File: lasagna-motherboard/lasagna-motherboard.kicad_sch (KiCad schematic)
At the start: 0 parts

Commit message: created IMU Schematic symbol
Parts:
- added U?: Adafruit_BNO055_IMU, symbol lasagna-motherboard:Adafruit_BNO055_IMU
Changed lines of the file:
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@@
 (kicad_sch (version 20211123) (generator eeschema)
   (paper "A4")
+  (symbol (lib_id "lasagna-motherboard:Adafruit_BNO055_IMU") (at 34.29 34.29 0) (unit 1)
+    (in_bom yes) (on_board yes) (fields_autoplaced)
+    (property "Reference" "U?" (id 0) (at 33.655 20.32 0))
+    (property "Value" "Adafruit_BNO055_IMU" (id 1) (at 33.655 22.86 0))
+    (property "Footprint" "" (id 2) (at 30.48 33.02 0)
+      (effects (font (size 1.27 1.27)) hide)
+    )
+    (property "Datasheet" "" (id 3) (at 30.48 33.02 0)
+      (effects (font (size 1.27 1.27)) hide)
+    )
+    (pin "1")
+    (pin "10")
+    (pin "2")
+    (pin "3")
+    (pin "4")
+    (pin "5")
+    (pin "6")
+    (pin "7")
+    (pin "8")
+    (pin "9")
+  )
   (sheet_instances
     (path "/" (page "1"))
   )
+  (symbol_instances
+    (path "/c659a157-8d7b-49bb-b1b7-529e35703d84"
+      (reference "U?") (unit 1) (value "Adafruit_BNO055_IMU") (footprint "")
+    )
+  )
 )

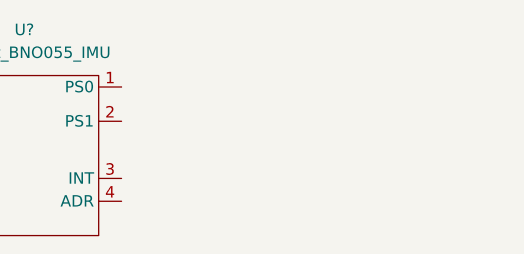
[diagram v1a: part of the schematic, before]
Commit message: added schematic symbol for FathomX and Jetson
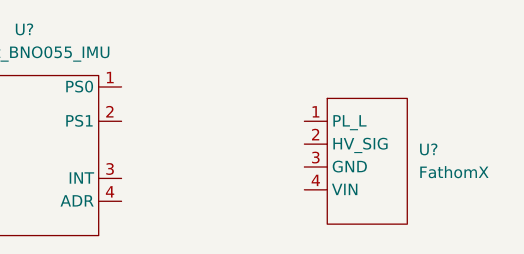
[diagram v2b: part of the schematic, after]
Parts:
- added U?: FathomX, symbol lasagna-motherboard:FathomX
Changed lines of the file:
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@@
     (pin "9")
+  )
+  (symbol (lib_id "lasagna-motherboard:FathomX") (at 71.12 34.29 0) (unit 1)
+    (in_bom yes) (on_board yes) (fields_autoplaced)
+    (property "Reference" "U?" (id 0) (at 77.47 33.6549 0)
+      (effects (font (size 1.27 1.27)) (justify left))
+    )
+    (property "Value" "FathomX" (id 1) (at 77.47 36.1949 0)
+      (effects (font (size 1.27 1.27)) (justify left))
+    )
+    (property "Footprint" "" (id 2) (at 66.04 30.48 0)
+      (effects (font (size 1.27 1.27)) hide)
+    )
+    (property "Datasheet" "" (id 3) (at 66.04 30.48 0)
+      (effects (font (size 1.27 1.27)) hide)
+    )
+    (pin "1")
+    (pin "2")
+    (pin "3")
+    (pin "4")
   )
   (sheet_instances
@@
       (reference "U?") (unit 1) (value "Adafruit_BNO055_IMU") (footprint "")
     )
+    (path "/cf27eb86-d6ed-48d5-bd7a-59210dc20ea2"
+      (reference "U?") (unit 1) (value "FathomX") (footprint "")
+    )
   )

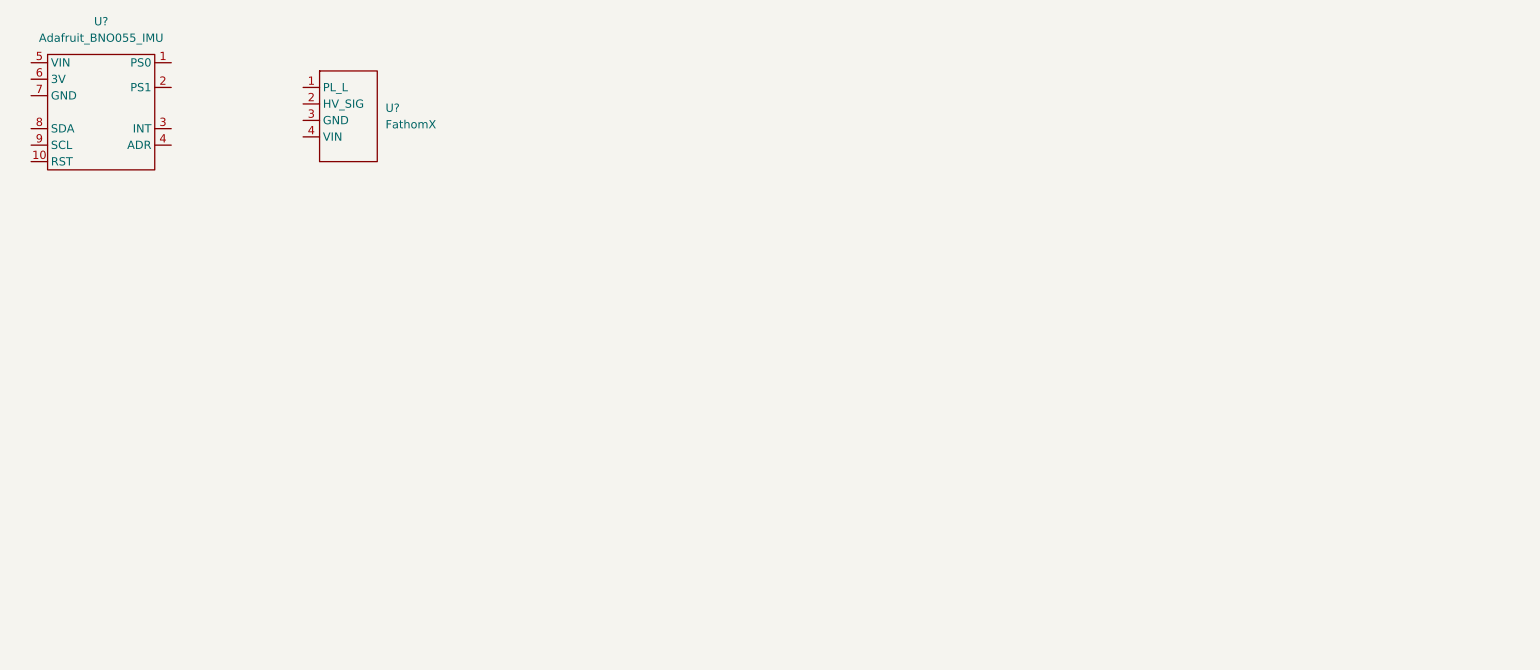
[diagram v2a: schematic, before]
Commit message: Created the Jetson Pin, power connector, and ESCSymbols
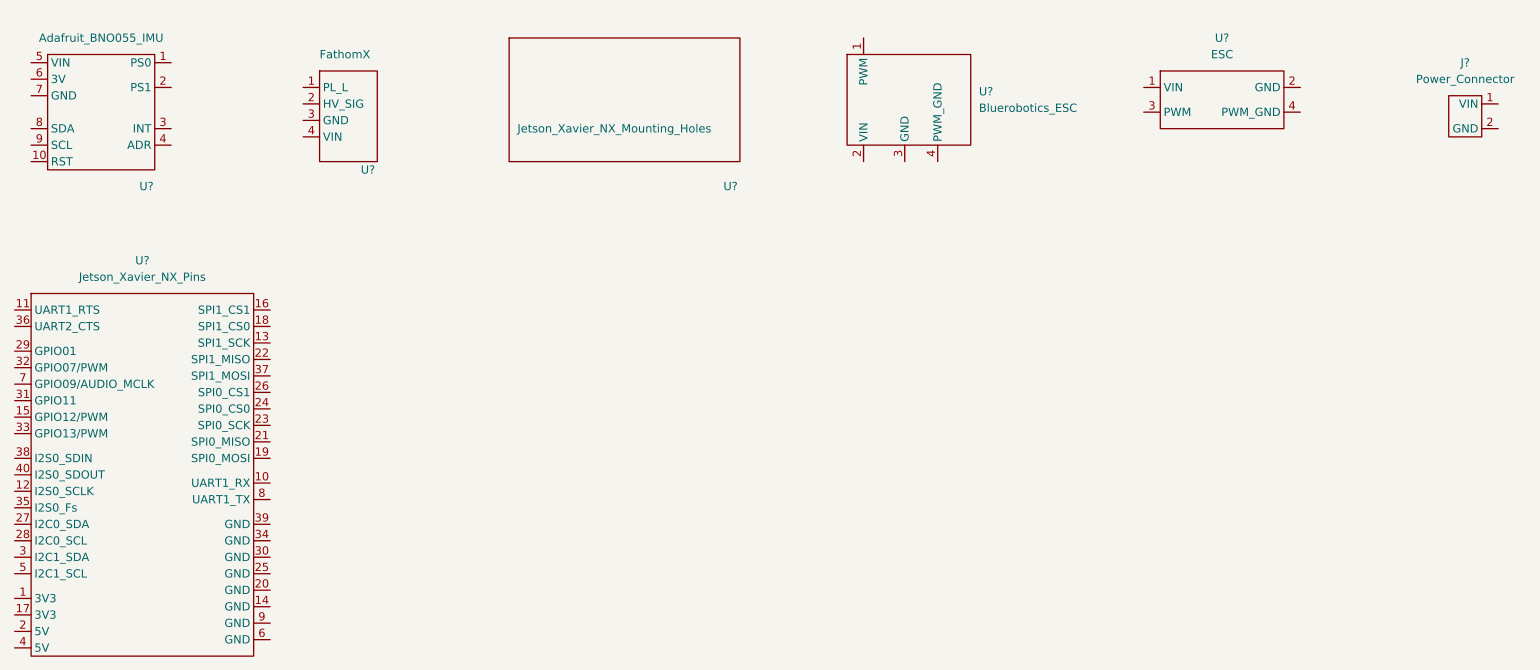
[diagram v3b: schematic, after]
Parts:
- added J?: Power_Connector, symbol lasagna-motherboard:Power_Connector
- added U?: Jetson_Xavier_NX_Mounting_Holes, symbol lasagna-motherboard:Jetson_Xavier_NX_Mounting_Holes
- added U?: Jetson_Xavier_NX_Pins, symbol lasagna-motherboard:Jetson_Xavier_NX_Pins
- added U?: Bluerobotics_ESC, symbol lasagna-motherboard:Bluerobotics_ESC
- added U?: ESC, symbol lasagna-motherboard:ESC
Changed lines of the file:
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@@
 (kicad_sch (version 20211123) (generator eeschema)
   (paper "A4")
+  (symbol (lib_id "lasagna-motherboard:Jetson_Xavier_NX_Mounting_Holes") (at 114.3 33.02 0) (unit 1)
+    (in_bom yes) (on_board yes)
+    (property "Reference" "U?" (id 0) (at 129.54 45.72 0)
+      (effects (font (size 1.27 1.27)) (justify left))
+    )
+    (property "Value" "Jetson_Xavier_NX_Mounting_Holes" (id 1) (at 97.79 36.83 0)
+      (effects (font (size 1.27 1.27)) (justify left))
+    )
+    (property "Footprint" "" (id 2) (at 114.3 33.02 0)
+      (effects (font (size 1.27 1.27)) hide)
+    )
+    (property "Datasheet" "" (id 3) (at 114.3 33.02 0)
+      (effects (font (size 1.27 1.27)) hide)
+    )
+  )
+  (symbol (lib_id "lasagna-motherboard:Jetson_Xavier_NX_Pins") (at 40.64 88.9 0) (unit 1)
+    (in_bom yes) (on_board yes) (fields_autoplaced)
+    (property "Reference" "U?" (id 0) (at 40.005 57.15 0))
+    (property "Value" "Jetson_Xavier_NX_Pins" (id 1) (at 40.005 59.69 0))
+    (property "Footprint" "" (id 2) (at 30.48 74.93 0)
+      (effects (font (size 1.27 1.27)) hide)
+    )
+    (property "Datasheet" "" (id 3) (at 30.48 74.93 0)
+      (effects (font (size 1.27 1.27)) hide)
+    )
+    (pin "1")
+    (pin "10")
+    (pin "11")
+    (pin "12")
+    (pin "13")
+    (pin "14")
+    (pin "15")
+    (pin "16")
+    (pin "17")
+    (pin "18")
+    (pin "19")
+    (pin "2")
+    (pin "20")
+    (pin "21")
+    (pin "22")
+    (pin "23")
+    (pin "24")
+    (pin "25")
+    (pin "26")
+    (pin "27")
+    (pin "28")
+    (pin "29")
+    (pin "3")
+    (pin "30")
+    (pin "31")
+    (pin "32")
+    (pin "33")
+    (pin "34")
+    (pin "35")
+    (pin "36")
+    (pin "37")
+    (pin "38")
+    (pin "39")
+    (pin "4")
+    (pin "40")
+    (pin "5")
+    (pin "6")
+    (pin "7")
+    (pin "8")
+    (pin "9")
+  )
+  (symbol (lib_id "lasagna-motherboard:Power_Connector") (at 243.84 34.29 0) (unit 1)
+    (in_bom yes) (on_board yes) (fields_autoplaced)
+    (property "Reference" "J?" (id 0) (at 243.84 26.67 0))
+    (property "Value" "Power_Connector" (id 1) (at 243.84 29.21 0))
+    (property "Footprint" "" (id 2) (at 246.38 33.02 0)
+      (effects (font (size 1.27 1.27)) hide)
+    )
+    (property "Datasheet" "" (id 3) (at 246.38 33.02 0)
+      (effects (font (size 1.27 1.27)) hide)
+    )
+    (pin "1")
+    (pin "2")
+  )
+  (symbol (lib_id "lasagna-motherboard:Bluerobotics_ESC") (at 160.02 29.21 0) (unit 1)
+    (in_bom yes) (on_board yes) (fields_autoplaced)
+    (property "Reference" "U?" (id 0) (at 168.91 31.1149 0)
+      (effects (font (size 1.27 1.27)) (justify left))
+    )
+    (property "Value" "Bluerobotics_ESC" (id 1) (at 168.91 33.6549 0)
+      (effects (font (size 1.27 1.27)) (justify left))
+    )
+    (property "Footprint" "" (id 2) (at 156.21 24.13 0)
+      (effects (font (size 1.27 1.27)) hide)
+    )
+    (property "Datasheet" "" (id 3) (at 156.21 24.13 0)
+      (effects (font (size 1.27 1.27)) hide)
+    )
+    (pin "1")
+    (pin "2")
+    (pin "3")
+    (pin "4")
+  )
   (symbol (lib_id "lasagna-motherboard:Adafruit_BNO055_IMU") (at 34.29 34.29 0) (unit 1)
-    (in_bom yes) (on_board yes) (fields_autoplaced)
-    (property "Reference" "U?" (id 0) (at 33.655 20.32 0))
+    (in_bom yes) (on_board yes)
+    (property "Reference" "U?" (id 0) (at 40.64 45.72 0))
     (property "Value" "Adafruit_BNO055_IMU" (id 1) (at 33.655 22.86 0))
     (property "Footprint" "" (id 2) (at 30.48 33.02 0)
@@
   )
   (symbol (lib_id "lasagna-motherboard:FathomX") (at 71.12 34.29 0) (unit 1)
-    (in_bom yes) (on_board yes) (fields_autoplaced)
-    (property "Reference" "U?" (id 0) (at 77.47 33.6549 0)
+    (in_bom yes) (on_board yes)
+    (property "Reference" "U?" (id 0) (at 73.66 43.18 0)
       (effects (font (size 1.27 1.27)) (justify left))
     )
-    (property "Value" "FathomX" (id 1) (at 77.47 36.1949 0)
+    (property "Value" "FathomX" (id 1) (at 67.31 25.4 0)
       (effects (font (size 1.27 1.27)) (justify left))
     )
@@
     (pin "4")
   )
+  (symbol (lib_id "lasagna-motherboard:ESC") (at 205.74 30.48 0) (unit 1)
+    (in_bom yes) (on_board yes) (fields_autoplaced)
+    (property "Reference" "U?" (id 0) (at 206.375 22.86 0))
+    (property "Value" "ESC" (id 1) (at 206.375 25.4 0))
+    (property "Footprint" "" (id 2) (at 205.74 30.48 0)
+      (effects (font (size 1.27 1.27)) hide)
+    )
+    (property "Datasheet" "" (id 3) (at 205.74 30.48 0)
+      (effects (font (size 1.27 1.27)) hide)
+    )
+    (pin "1")
+    (pin "2")
+    (pin "3")
+    (pin "4")
+  )
   (sheet_instances
     (path "/" (page "1"))
   )
   (symbol_instances
+    (path "/9b8b9a1b-a1ca-47f4-ab33-f59a78659b22"
+      (reference "J?") (unit 1) (value "Power_Connector") (footprint "")
+    )
+    (path "/1f7ea3dc-e040-4340-ac71-367bf56dbd36"
+      (reference "U?") (unit 1) (value "Jetson_Xavier_NX_Mounting_Holes") (footprint "")
+    )
+    (path "/968fa752-f8dc-4cee-8837-7c67c93064bc"
+      (reference "U?") (unit 1) (value "Jetson_Xavier_NX_Pins") (footprint "")
+    )
+    (path "/ac3a7bdc-0639-4137-93c2-0f632930b94b"
+      (reference "U?") (unit 1) (value "Bluerobotics_ESC") (footprint "")
+    )
     (path "/c659a157-8d7b-49bb-b1b7-529e35703d84"
       (reference "U?") (unit 1) (value "Adafruit_BNO055_IMU") (footprint "")
@@
       (reference "U?") (unit 1) (value "FathomX") (footprint "")
     )
+    (path "/e447f43b-8f82-4ceb-87ae-0aec8d2a9782"
+      (reference "U?") (unit 1) (value "ESC") (footprint "")
+    )
   )
